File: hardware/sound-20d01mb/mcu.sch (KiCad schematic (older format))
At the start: 26 parts

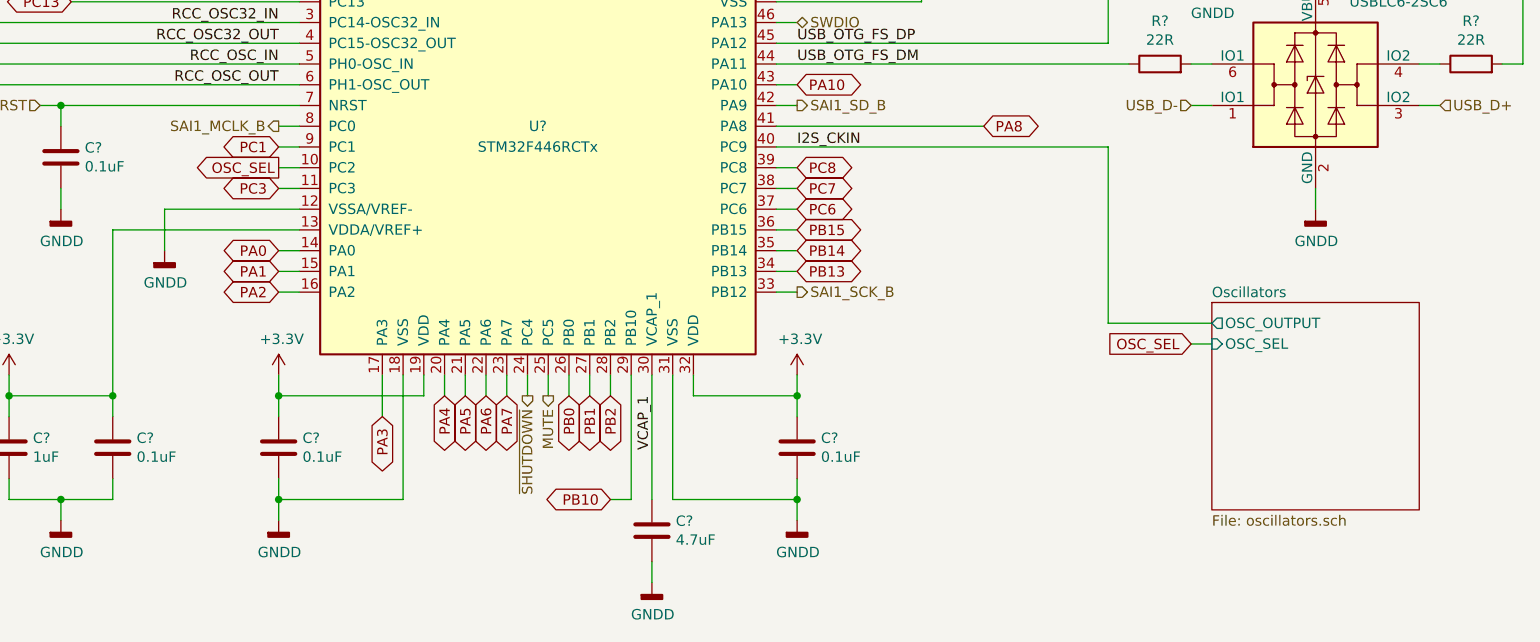
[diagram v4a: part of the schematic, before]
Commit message: Removed oscillators.sch
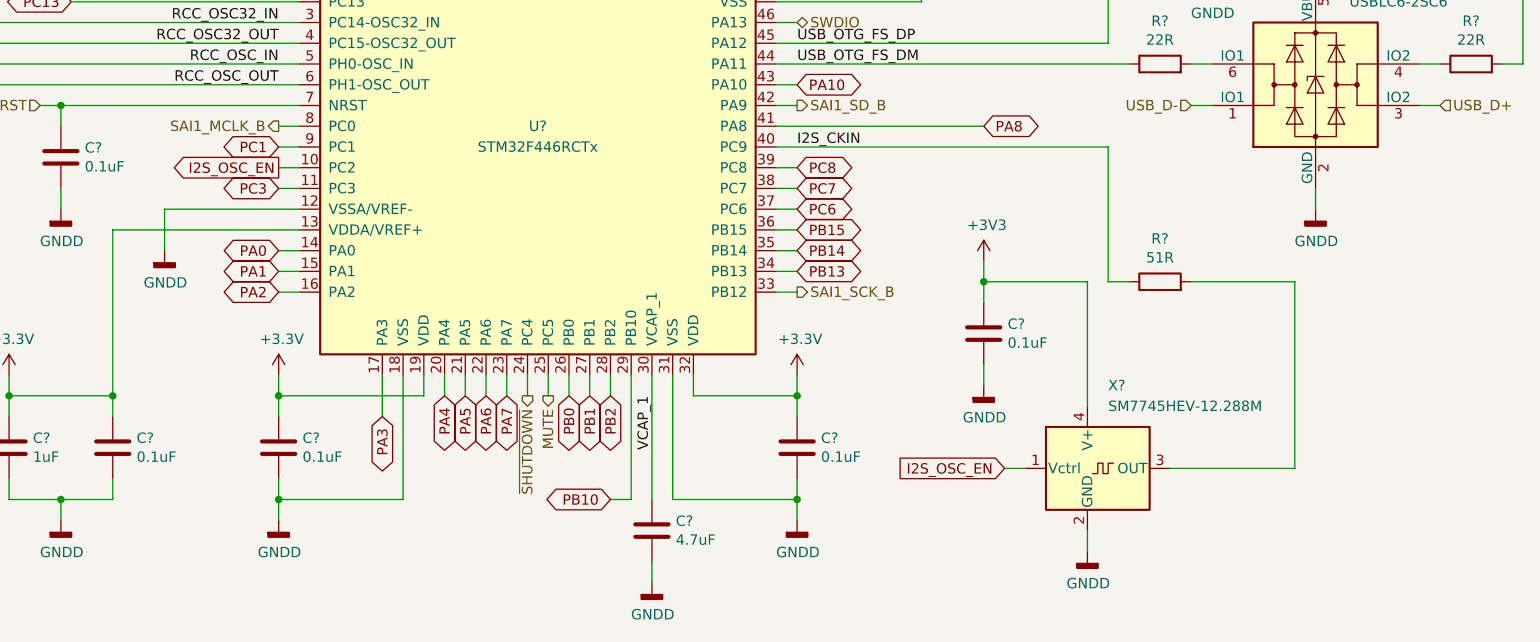
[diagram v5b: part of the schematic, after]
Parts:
- added C?: 0.1uF, Capacitor_SMD:C_1206_3216Metric_Pad1.42x1.75mm_HandSolder, symbol Device:C
- added R?: 51R, Resistor_SMD:R_1206_3216Metric_Pad1.42x1.75mm_HandSolder, symbol Device:R
- added X?: SM7745HEV-12.288M, Oscillator:Oscillator_SMD_Fordahl_DFAS2-4Pin_7.3x5.1mm_HandSoldering, symbol Oscillator:DFA-S2
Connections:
- net +3V3: now also C?.1, X?.4 (V+)
- net GNDD: now also C?.2, X?.2 (GND)
- net I2S_CKIN: now also R?.1
- net OSC_SEL renamed I2S_OSC_EN
- net I2S_OSC_EN: now also X?.1 (Vctrl)
- new net: R?.2, X?.3 (OUT)
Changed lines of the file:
@@
 $Descr A4 11693 8268
 encoding utf-8
-Sheet 2 6
+Sheet 2 5
 Title "Sound-20D01MB"
 Date "2021-07-01"
@@
 	1    0    0    -1
 $EndComp
-$Sheet
-S 8700 4600 1000 1000
-U 612AF97F
-F0 "Oscillators" 50
-F1 "oscillators.sch" 50
-F2 "OSC_OUTPUT" O L 8700 4700 50
-F3 "OSC_SEL" I L 8700 4800 50
-$EndSheet
-Wire Wire Line
-	8700 4700 8200 4700
-Wire Wire Line
-	8200 4700 8200 3850
 Wire Wire Line
 	8200 3850 6600 3850
@@
 I2S_CKIN
 Text GLabel 4200 3950 0    50   Output ~ 0
-OSC_SEL
+I2S_OSC_EN
 Wire Wire Line
 	4300 3950 4200 3950
-Text GLabel 8600 4800 0    50   Input ~ 0
-OSC_SEL
-Wire Wire Line
-	8600 4800 8700 4800
+Text GLabel 7700 5400 0    50   Input ~ 0
+I2S_OSC_EN
 Wire Wire Line
 	5300 2650 5300 2550
@@
 Wire Notes Line
 	8700 1800 8700 1050
+$Comp
+L Oscillator:DFA-S2 X?
+U 1 1 619CF940
+P 8100 5400
+AR Path="/60DE2DEE/612AF97F/619CF940" Ref="X?"  Part="1"
+AR Path="/60DE2DEE/619CF940" Ref="X?"  Part="1"
+F 0 "X?" H 8200 5800 50  0000 L CNN
+F 1 "SM7745HEV-12.288M" H 8200 5700 50  0000 L CNN
+F 2 "Oscillator:Oscillator_SMD_Fordahl_DFAS2-4Pin_7.3x5.1mm_HandSoldering" H 9200 5050 50  0001 C CNN
+F 3 "http://www.metatech.com.hk/product/fordahl/pdf/2002%20TCXO%20Page%2043-58.pdf" H 8000 5400 50  0001 C CNN
+	1    8100 5400
+	1    0    0    -1
+$EndComp
+$Comp
+L Device:R R?
+U 1 1 619CF947
+P 8450 4500
+AR Path="/60DE2DEE/612AF97F/619CF947" Ref="R?"  Part="1"
+AR Path="/60DE2DEE/619CF947" Ref="R?"  Part="1"
+F 0 "R?" V 8657 4500 50  0000 C CNN
+F 1 "51R" V 8566 4500 50  0000 C CNN
+F 2 "Resistor_SMD:R_1206_3216Metric_Pad1.42x1.75mm_HandSolder" V 8380 4500 50  0001 C CNN
+F 3 "~" H 8450 4500 50  0001 C CNN
+	1    8450 4500
+	0    -1   -1   0
+$EndComp
+$Comp
+L power:GNDD #PWR?
+U 1 1 619CF950
+P 8100 5800
+AR Path="/60DE2DEE/612AF97F/619CF950" Ref="#PWR?"  Part="1"
+AR Path="/60DE2DEE/619CF950" Ref="#PWR?"  Part="1"
+F 0 "#PWR?" H 8100 5550 50  0001 C CNN
+F 1 "GNDD" H 8104 5645 50  0000 C CNN
+F 2 "" H 8100 5800 50  0001 C CNN
+F 3 "" H 8100 5800 50  0001 C CNN
+	1    8100 5800
+	1    0    0    -1
+$EndComp
+Wire Wire Line
+	8100 5700 8100 5800
+$Comp
+L power:+3V3 #PWR?
+U 1 1 619CF957
+P 7600 4400
+AR Path="/60DE2DEE/612AF97F/619CF957" Ref="#PWR?"  Part="1"
+AR Path="/60DE2DEE/619CF957" Ref="#PWR?"  Part="1"
+F 0 "#PWR?" H 7600 4250 50  0001 C CNN
+F 1 "+3V3" H 7615 4573 50  0000 C CNN
+F 2 "" H 7600 4400 50  0001 C CNN
+F 3 "" H 7600 4400 50  0001 C CNN
+	1    7600 4400
+	1    0    0    -1
+$EndComp
+$Comp
+L Device:C C?
+U 1 1 619CF95D
+P 7600 4750
+AR Path="/60DE2DEE/612AF97F/619CF95D" Ref="C?"  Part="1"
+AR Path="/60DE2DEE/619CF95D" Ref="C?"  Part="1"
+F 0 "C?" H 7715 4796 50  0000 L CNN
+F 1 "0.1uF" H 7715 4705 50  0000 L CNN
+F 2 "Capacitor_SMD:C_1206_3216Metric_Pad1.42x1.75mm_HandSolder" H 7638 4600 50  0001 C CNN
+F 3 "~" H 7600 4750 50  0001 C CNN
+	1    7600 4750
+	1    0    0    -1
+$EndComp
+Wire Wire Line
+	7600 4600 7600 4500
+$Comp
+L power:GNDD #PWR?
+U 1 1 619CF965
+P 7600 5000
+AR Path="/60DE2DEE/612AF97F/619CF965" Ref="#PWR?"  Part="1"
+AR Path="/60DE2DEE/619CF965" Ref="#PWR?"  Part="1"
+F 0 "#PWR?" H 7600 4750 50  0001 C CNN
+F 1 "GNDD" H 7604 4845 50  0000 C CNN
+F 2 "" H 7600 5000 50  0001 C CNN
+F 3 "" H 7600 5000 50  0001 C CNN
+	1    7600 5000
+	1    0    0    -1
+$EndComp
+Wire Wire Line
+	7600 4900 7600 5000
+Wire Wire Line
+	7600 4500 8100 4500
+Connection ~ 7600 4500
+Wire Wire Line
+	7600 4500 7600 4400
+Wire Wire Line
+	7800 5400 7700 5400
+Wire Wire Line
+	8100 4500 8100 5100
+Wire Wire Line
+	8300 4500 8200 4500
+Wire Wire Line
+	8600 4500 9100 4500
+Wire Wire Line
+	9100 4500 9100 5400
+Wire Wire Line
+	9100 5400 8500 5400
+Wire Wire Line
+	8200 3850 8200 4500
 $EndSCHEMATC

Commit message: Added datasheet for sm77h
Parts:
- removed X?: SM7745HEV-12.288M, Oscillator:Oscillator_SMD_Fordahl_DFAS2-4Pin_7.3x5.1mm_HandSoldering, symbol Oscillator:DFA-S2
- added X?: SM7745HEV-12.288M, Oscillator:Oscillator_SMD_Fordahl_DFAS2-4Pin_7.3x5.1mm_HandSoldering, symbol Oscillator:XO91
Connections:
- net +3V3: now also X?.4 (V+)
- net GNDD: now also X?.2 (GND)
- net I2S_OSC_EN: now also X?.1 (EN)
- net at R?.2: now also X?.3 (OUT)
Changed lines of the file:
@@
 	8700 1800 8700 1050
-$Comp
-L Oscillator:DFA-S2 X?
-U 1 1 619CF940
-P 8100 5400
-AR Path="/60DE2DEE/612AF97F/619CF940" Ref="X?"  Part="1"
-AR Path="/60DE2DEE/619CF940" Ref="X?"  Part="1"
-F 0 "X?" H 8200 5800 50  0000 L CNN
-F 1 "SM7745HEV-12.288M" H 8200 5700 50  0000 L CNN
-F 2 "Oscillator:Oscillator_SMD_Fordahl_DFAS2-4Pin_7.3x5.1mm_HandSoldering" H 9200 5050 50  0001 C CNN
-F 3 "http://www.metatech.com.hk/product/fordahl/pdf/2002%20TCXO%20Page%2043-58.pdf" H 8000 5400 50  0001 C CNN
-	1    8100 5400
-	1    0    0    -1
-$EndComp
 $Comp
 L Device:R R?
@@
 	9100 4500 9100 5400
 Wire Wire Line
-	9100 5400 8500 5400
+	9100 5400 8400 5400
 Wire Wire Line
 	8200 3850 8200 4500
+$Comp
+L Oscillator:XO91 X?
+U 1 1 619CCBD0
+P 8100 5400
+F 0 "X?" H 8600 5800 50  0000 C CNN
+F 1 "SM7745HEV-12.288M" H 8600 5700 50  0000 C CNN
+F 2 "Oscillator:Oscillator_SMD_Fordahl_DFAS2-4Pin_7.3x5.1mm_HandSoldering" H 8800 5050 50  0001 C CNN
+F 3 "http://www.pletronics.com/uploads/datasheets/sm77h%203.3v.pdf" H 8000 5400 50  0001 C CNN
+	1    8100 5400
+	1    0    0    -1
+$EndComp
 $EndSCHEMATC

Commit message: Annotate schematic
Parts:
- gave numbers to parts that had none: 29
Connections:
- net RTC_VBAT renamed +BATT
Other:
- moved on the sheet: C1, JP2
